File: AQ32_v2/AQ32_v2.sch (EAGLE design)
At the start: 115 parts, among them Q2 BCV27, Q3 BCV27, Q5 BCV27, Q6 BCV27, U1 ITG-3200, U10 MS5611, U11 MIC5239, U13 74AHC1G86DCK, U2 STM32F10XVXT6, U3 74AHC1G86DCK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

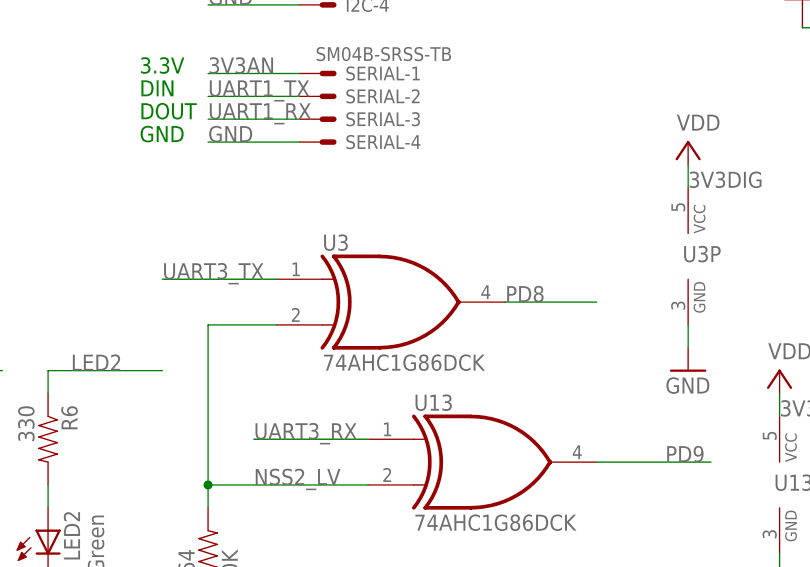
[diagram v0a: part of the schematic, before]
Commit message: fixed SBUS Tx connection, fixed clearance issue with updated XOR connections, added extra vias for ground
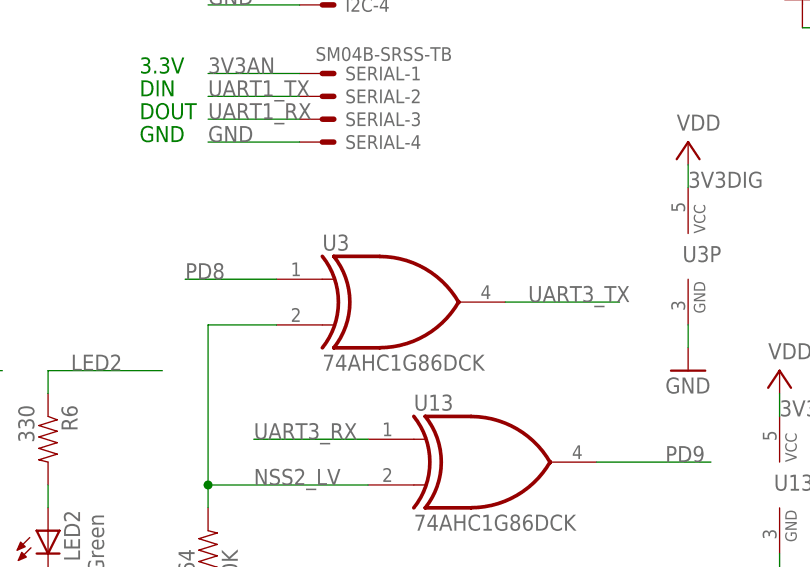
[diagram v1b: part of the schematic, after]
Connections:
- net PD8: now also U3A.I0; no longer U3A.O
- net UART3_TX: now also U3A.O; no longer U3A.I0
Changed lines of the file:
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@@
 </segment>
 <segment>
-<pinref part="U3" gate="A" pin="I0"/>
-<wire x1="83.82" y1="45.72" x2="71.12" y2="45.72" width="0.1524" layer="91"/>
-<label x="71.12" y="45.72" size="1.778" layer="95"/>
+<pinref part="U3" gate="A" pin="O"/>
+<wire x1="109.22" y1="43.18" x2="121.92" y2="43.18" width="0.1524" layer="91"/>
+<label x="111.76" y="43.18" size="1.778" layer="95"/>
 </segment>
 </net>
@@
 </segment>
 <segment>
-<pinref part="U3" gate="A" pin="O"/>
-<wire x1="109.22" y1="43.18" x2="119.38" y2="43.18" width="0.1524" layer="91"/>
-<label x="109.22" y="43.18" size="1.778" layer="95"/>
-</segment>
-</net>
+<pinref part="U3" gate="A" pin="I0"/>
+<wire x1="83.82" y1="45.72" x2="73.66" y2="45.72" width="0.1524" layer="91"/>
+<label x="73.66" y="45.72" size="1.778" layer="95"/>
+</segment>
+</net>

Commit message: "j" version from Alfred
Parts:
- JP1: value (none) -> JP1; device SparkFun-Connectors:M02PTH -> SparkFun-Connectors:M02LOCK
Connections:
- net 3V3AN: now also C29.1, C45.1, U1.VDD, U10.CSB, U10.CSB@2, U10.PS, U10.VDD; no longer I2C-1.S, JP1-2.7, JP1-2.8, SERIAL-1.S
- net 3V3DIG: now also I2C-1.S, JP1-2.7, JP1-2.8, SERIAL-1.S; no longer C29.1, C45.1, U1.VDD, U10.CSB, U10.CSB@2, U10.PS, U10.VDD
- net LEDGND1: now also Q2.C; no longer Q5.C
- net LEDGND2: now also Q5.C; no longer Q2.C
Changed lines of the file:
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@@
 <part name="U10" library="DSP-TI" deviceset="MS5611" device=""/>
 <part name="SUPPLY19" library="supply2" deviceset="GND" device=""/>
-<part name="SUPPLY20" library="supply2" deviceset="VDD" device=""/>
 <part name="C45" library="rcl" deviceset="C-US" device="C0402" value="0.1uF"/>
 <part name="SUPPLY21" library="supply2" deviceset="GND" device=""/>
@@
 <part name="GND25" library="SparkFun" deviceset="GND" device=""/>
 <part name="SUPPLY2" library="supply2" deviceset="V+" device="" value="VDD"/>
-<part name="JP1" library="SparkFun-Connectors" deviceset="M02" device="PTH"/>
+<part name="JP1" library="SparkFun-Connectors" deviceset="M02" device="LOCK" value="JP1"/>
+<part name="P+4" library="SparkFun" deviceset="3.3V" device="" value="VDDA"/>
 </parts>
 <sheets>
@@
 <instance part="U10" gate="G$1" x="307.34" y="33.02"/>
 <instance part="SUPPLY19" gate="GND" x="309.88" y="10.16"/>
-<instance part="SUPPLY20" gate="G$1" x="309.88" y="60.96"/>
 <instance part="C45" gate="G$1" x="325.12" y="50.8"/>
 <instance part="SUPPLY21" gate="GND" x="325.12" y="40.64"/>
@@
 <instance part="SUPPLY2" gate="1" x="129.54" y="60.96"/>
 <instance part="JP1" gate="G$1" x="17.78" y="99.06"/>
+<instance part="P+4" gate="G$1" x="309.88" y="58.42"/>
 </instances>
 <busses>
@@
 <pinref part="R3" gate="G$1" pin="1"/>
 <pinref part="GND15" gate="1" pin="GND"/>
-<pinref part="JP1" gate="G$1" pin="1"/>
 <wire x1="33.02" y1="73.66" x2="33.02" y2="71.12" width="0.1524" layer="91"/>
 <wire x1="25.4" y1="99.06" x2="27.94" y2="99.06" width="0.1524" layer="91"/>
@@
 <wire x1="27.94" y1="73.66" x2="33.02" y2="73.66" width="0.1524" layer="91"/>
 <junction x="33.02" y="73.66"/>
+<pinref part="JP1" gate="G$1" pin="1"/>
 </segment>
 <segment>
@@
 </segment>
 <segment>
-<pinref part="SERIAL" gate="-1" pin="S"/>
-<wire x1="86.36" y1="68.58" x2="76.2" y2="68.58" width="0.1524" layer="91"/>
-<label x="76.2" y="68.58" size="1.778" layer="95"/>
-</segment>
-<segment>
-<pinref part="I2C" gate="-1" pin="S"/>
-<wire x1="86.36" y1="83.82" x2="76.2" y2="83.82" width="0.1524" layer="91"/>
-<label x="76.2" y="83.82" size="1.778" layer="95"/>
-</segment>
-<segment>
-<pinref part="JP1-2" gate="G$1" pin="8"/>
-<wire x1="429.26" y1="76.2" x2="436.88" y2="76.2" width="0.1524" layer="91"/>
-<label x="429.26" y="76.2" size="1.778" layer="95"/>
-</segment>
-<segment>
-<pinref part="JP1-2" gate="G$1" pin="7"/>
-<wire x1="429.26" y1="73.66" x2="436.88" y2="73.66" width="0.1524" layer="91"/>
-<label x="429.26" y="73.66" size="1.778" layer="95"/>
+<wire x1="309.88" y1="58.42" x2="309.88" y2="55.88" width="0.1524" layer="91"/>
+<wire x1="309.88" y1="55.88" x2="309.88" y2="50.8" width="0.1524" layer="91"/>
+<wire x1="309.88" y1="55.88" x2="325.12" y2="55.88" width="0.1524" layer="91"/>
+<wire x1="325.12" y1="55.88" x2="325.12" y2="53.34" width="0.1524" layer="91"/>
+<junction x="309.88" y="55.88"/>
+<pinref part="U10" gate="G$1" pin="VDD"/>
+<pinref part="C45" gate="G$1" pin="1"/>
+<label x="309.88" y="58.42" size="1.778" layer="95"/>
+<wire x1="309.88" y1="55.88" x2="281.94" y2="55.88" width="0.1524" layer="91"/>
+<wire x1="281.94" y1="55.88" x2="281.94" y2="40.64" width="0.1524" layer="91"/>
+<pinref part="U10" gate="G$1" pin="CSB@2"/>
+<wire x1="281.94" y1="40.64" x2="281.94" y2="38.1" width="0.1524" layer="91"/>
+<wire x1="281.94" y1="38.1" x2="281.94" y2="35.56" width="0.1524" layer="91"/>
+<wire x1="281.94" y1="35.56" x2="292.1" y2="35.56" width="0.1524" layer="91"/>
+<pinref part="U10" gate="G$1" pin="CSB"/>
+<wire x1="292.1" y1="38.1" x2="281.94" y2="38.1" width="0.1524" layer="91"/>
+<pinref part="U10" gate="G$1" pin="PS"/>
+<wire x1="292.1" y1="40.64" x2="281.94" y2="40.64" width="0.1524" layer="91"/>
+<junction x="281.94" y="40.64"/>
+<junction x="281.94" y="38.1"/>
+<pinref part="P+4" gate="G$1" pin="3.3V"/>
+</segment>
+<segment>
+<wire x1="342.9" y1="157.48" x2="327.66" y2="157.48" width="0.1524" layer="91"/>
+<wire x1="342.9" y1="157.48" x2="342.9" y2="149.86" width="0.1524" layer="91"/>
+<junction x="327.66" y="157.48"/>
+<label x="330.2" y="157.48" size="1.778" layer="95"/>
+<pinref part="U1" gate="G$1" pin="VDD"/>
+<pinref part="C29" gate="G$1" pin="1"/>
 </segment>
 </net>
@@
 </segment>
 <segment>
-<wire x1="309.88" y1="58.42" x2="309.88" y2="55.88" width="0.1524" layer="91"/>
-<wire x1="309.88" y1="55.88" x2="309.88" y2="50.8" width="0.1524" layer="91"/>
-<wire x1="309.88" y1="55.88" x2="325.12" y2="55.88" width="0.1524" layer="91"/>
-<wire x1="325.12" y1="55.88" x2="325.12" y2="53.34" width="0.1524" layer="91"/>
-<junction x="309.88" y="55.88"/>
-<pinref part="SUPPLY20" gate="G$1" pin="VDD"/>
-<pinref part="U10" gate="G$1" pin="VDD"/>
-<pinref part="C45" gate="G$1" pin="1"/>
-<label x="309.88" y="58.42" size="1.778" layer="95"/>
-<wire x1="309.88" y1="55.88" x2="281.94" y2="55.88" width="0.1524" layer="91"/>
-<wire x1="281.94" y1="55.88" x2="281.94" y2="40.64" width="0.1524" layer="91"/>
-<pinref part="U10" gate="G$1" pin="CSB@2"/>
-<wire x1="281.94" y1="40.64" x2="281.94" y2="38.1" width="0.1524" layer="91"/>
-<wire x1="281.94" y1="38.1" x2="281.94" y2="35.56" width="0.1524" layer="91"/>
-<wire x1="281.94" y1="35.56" x2="292.1" y2="35.56" width="0.1524" layer="91"/>
-<pinref part="U10" gate="G$1" pin="CSB"/>
-<wire x1="292.1" y1="38.1" x2="281.94" y2="38.1" width="0.1524" layer="91"/>
-<pinref part="U10" gate="G$1" pin="PS"/>
-<wire x1="292.1" y1="40.64" x2="281.94" y2="40.64" width="0.1524" layer="91"/>
-<junction x="281.94" y="40.64"/>
-<junction x="281.94" y="38.1"/>
-</segment>
-<segment>
-<wire x1="342.9" y1="157.48" x2="327.66" y2="157.48" width="0.1524" layer="91"/>
-<wire x1="342.9" y1="157.48" x2="342.9" y2="149.86" width="0.1524" layer="91"/>
-<junction x="327.66" y="157.48"/>
-<label x="330.2" y="157.48" size="1.778" layer="95"/>
-<pinref part="U1" gate="G$1" pin="VDD"/>
-<pinref part="C29" gate="G$1" pin="1"/>
-</segment>
-<segment>
 <wire x1="261.62" y1="170.18" x2="261.62" y2="175.26" width="0.1524" layer="91"/>
 <label x="259.08" y="175.26" size="1.778" layer="95"/>
@@
 <pinref part="U3" gate="P" pin="VCC"/>
 <label x="129.54" y="55.88" size="1.778" layer="95"/>
+</segment>
+<segment>
+<pinref part="I2C" gate="-1" pin="S"/>
+<wire x1="86.36" y1="83.82" x2="76.2" y2="83.82" width="0.1524" layer="91"/>
+<label x="76.2" y="83.82" size="1.778" layer="95"/>
+</segment>
+<segment>
+<pinref part="SERIAL" gate="-1" pin="S"/>
+<wire x1="86.36" y1="68.58" x2="76.2" y2="68.58" width="0.1524" layer="91"/>
+<label x="76.2" y="68.58" size="1.778" layer="95"/>
+</segment>
+<segment>
+<pinref part="JP1-2" gate="G$1" pin="8"/>
+<wire x1="429.26" y1="76.2" x2="436.88" y2="76.2" width="0.1524" layer="91"/>
+<label x="429.26" y="76.2" size="1.778" layer="95"/>
+</segment>
+<segment>
+<pinref part="JP1-2" gate="G$1" pin="7"/>
+<wire x1="429.26" y1="73.66" x2="436.88" y2="73.66" width="0.1524" layer="91"/>
+<label x="429.26" y="73.66" size="1.778" layer="95"/>
 </segment>
 </net>
@@
 <net name="LEDGND1" class="0">
 <segment>
+<pinref part="JP4-1" gate="G$1" pin="1"/>
+<wire x1="495.3" y1="25.4" x2="505.46" y2="25.4" width="0.1524" layer="91"/>
+<label x="495.3" y="25.4" size="1.778" layer="95"/>
+</segment>
+<segment>
+<wire x1="30.48" y1="33.02" x2="27.94" y2="33.02" width="0.1524" layer="91"/>
+<pinref part="Q2" gate="G$1" pin="C"/>
+<label x="27.94" y="33.02" size="1.778" layer="95"/>
+</segment>
+</net>
+<net name="LEDGND2" class="0">
+<segment>
+<pinref part="JP4-1" gate="G$1" pin="2"/>
+<wire x1="495.3" y1="27.94" x2="505.46" y2="27.94" width="0.1524" layer="91"/>
+<label x="495.3" y="27.94" size="1.778" layer="95"/>
+</segment>
+<segment>
 <wire x1="30.48" y1="45.72" x2="27.94" y2="45.72" width="0.1524" layer="91"/>
 <pinref part="Q5" gate="G$1" pin="C"/>
 <label x="27.94" y="45.72" size="1.778" layer="95"/>
 </segment>
-<segment>
-<pinref part="JP4-1" gate="G$1" pin="1"/>
-<wire x1="495.3" y1="25.4" x2="505.46" y2="25.4" width="0.1524" layer="91"/>
-<label x="495.3" y="25.4" size="1.778" layer="95"/>
-</segment>
-</net>
-<net name="LEDGND2" class="0">
-<segment>
-<wire x1="30.48" y1="33.02" x2="27.94" y2="33.02" width="0.1524" layer="91"/>
-<pinref part="Q2" gate="G$1" pin="C"/>
-<label x="27.94" y="33.02" size="1.778" layer="95"/>
-</segment>
-<segment>
-<pinref part="JP4-1" gate="G$1" pin="2"/>
-<wire x1="495.3" y1="27.94" x2="505.46" y2="27.94" width="0.1524" layer="91"/>
-<label x="495.3" y="27.94" size="1.778" layer="95"/>
-</segment>
-</net>
+</net>

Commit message: change LED connector type for normal 100mil pitch
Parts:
- JP1, JP4-1, JP4-2: device SparkFun-Connectors:M02LOCK -> SparkFun-Connectors:M02PTH
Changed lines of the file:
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@@
 <part name="OSD" library="con-jst2" deviceset="?M07B-SRSS-TB" device="S"/>
 <part name="L2" library="SparkFun" deviceset="INDUCTOR" device="0805" value="22uH"/>
-<part name="JP4-1" library="SparkFun-Connectors" deviceset="M02" device="LOCK" value="JP4"/>
-<part name="JP4-2" library="SparkFun-Connectors" deviceset="M02" device="LOCK" value="JP4"/>
+<part name="JP4-1" library="SparkFun-Connectors" deviceset="M02" device="PTH" value="JP4"/>
+<part name="JP4-2" library="SparkFun-Connectors" deviceset="M02" device="PTH" value="JP4"/>
 <part name="JP3-1" library="SparkFun-Connectors" deviceset="M09" device=""/>
 <part name="JP3-2" library="SparkFun-Connectors" deviceset="M09" device=""/>
@@
 <part name="GND25" library="SparkFun" deviceset="GND" device=""/>
 <part name="SUPPLY2" library="supply2" deviceset="V+" device="" value="VDD"/>
-<part name="JP1" library="SparkFun-Connectors" deviceset="M02" device="LOCK" value="JP1"/>
+<part name="JP1" library="SparkFun-Connectors" deviceset="M02" device="PTH" value="JP1"/>
 <part name="P+4" library="SparkFun" deviceset="3.3V" device="" value="VDDA"/>
 </parts>

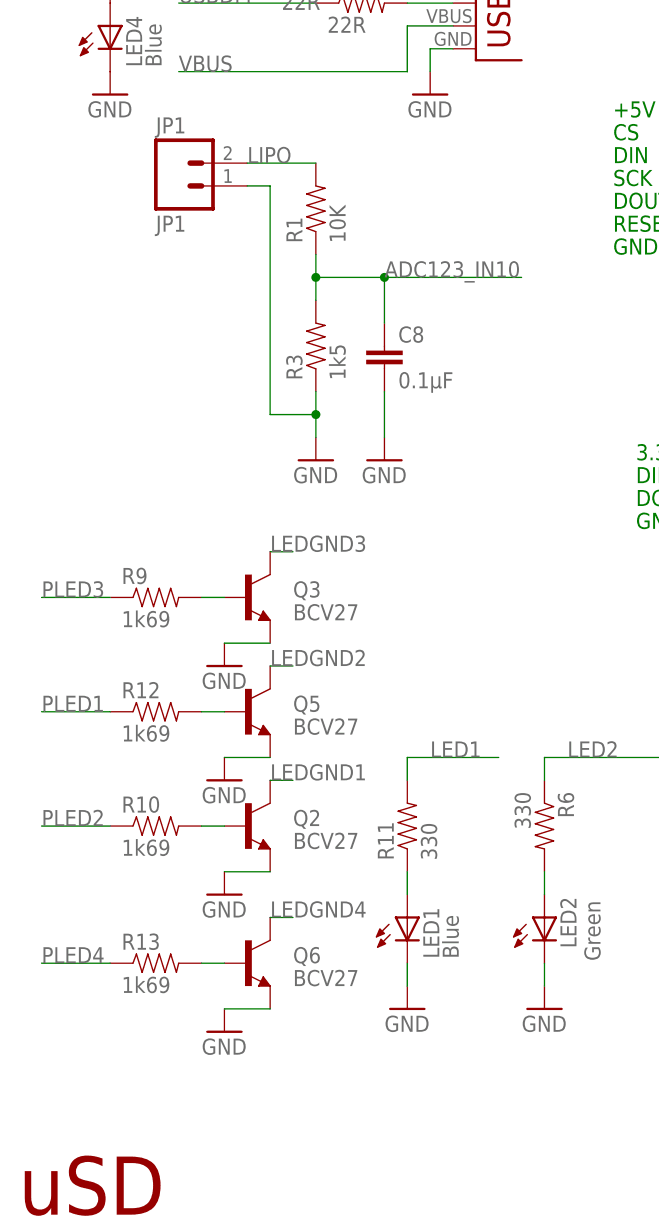
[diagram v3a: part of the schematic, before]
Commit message: Isolate BM/LED GND from main GND using 0R resistor. More clearance around holes.
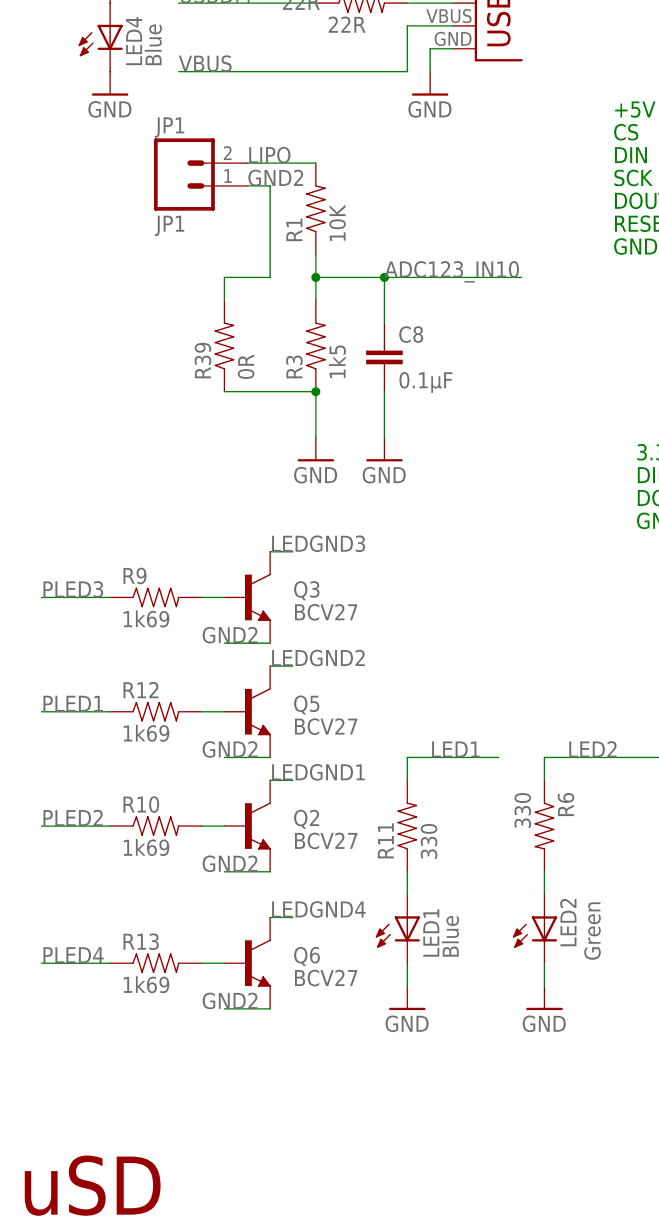
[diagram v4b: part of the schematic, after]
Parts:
- added R39: 0R, SparkFun:RESISTOR0402
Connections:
- new net GND2: JP1.1, Q2.E, Q3.E, Q5.E, Q6.E, R39.2
- net GND: now also R39.1; no longer JP1.1, Q2.E, Q3.E, Q5.E, Q6.E
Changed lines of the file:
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@@
 <part name="GND16" library="supply1" deviceset="GND" device=""/>
 <part name="SUPPLY7" library="supply2" deviceset="VDD" device=""/>
-<part name="GND47" library="SparkFun" deviceset="GND" device=""/>
-<part name="GND48" library="SparkFun" deviceset="GND" device=""/>
-<part name="GND49" library="SparkFun" deviceset="GND" device=""/>
-<part name="GND50" library="SparkFun" deviceset="GND" device=""/>
 <part name="U13" library="74xx-little-us" deviceset="74*1G86" device="DCK" technology="AHC"/>
 <part name="GND51" library="SparkFun" deviceset="GND" device=""/>
@@
 <part name="JP1" library="SparkFun-Connectors" deviceset="M02" device="PTH" value="JP1"/>
 <part name="P+4" library="SparkFun" deviceset="3.3V" device="" value="VDDA"/>
+<part name="R39" library="SparkFun" deviceset="RESISTOR" device="0402" value="0R"/>
 </parts>
 <sheets>
@@
 <instance part="GND16" gate="1" x="124.46" y="-55.88"/>
 <instance part="SUPPLY7" gate="G$1" x="147.32" y="-25.4"/>
-<instance part="GND47" gate="1" x="22.86" y="5.08"/>
-<instance part="GND48" gate="1" x="22.86" y="20.32"/>
-<instance part="GND49" gate="1" x="22.86" y="33.02"/>
-<instance part="GND50" gate="1" x="22.86" y="45.72"/>
 <instance part="U13" gate="A" x="106.68" y="25.4"/>
 <instance part="U13" gate="P" x="139.7" y="22.86"/>
@@
 <instance part="JP1" gate="G$1" x="17.78" y="99.06"/>
 <instance part="P+4" gate="G$1" x="309.88" y="58.42"/>
+<instance part="R39" gate="G$1" x="22.86" y="81.28" rot="R90"/>
 </instances>
 <busses>
@@
 </segment>
 <segment>
-<wire x1="33.02" y1="76.2" x2="33.02" y2="73.66" width="0.1524" layer="91"/>
+<pinref part="GND15" gate="1" pin="GND"/>
 <pinref part="R3" gate="G$1" pin="1"/>
-<pinref part="GND15" gate="1" pin="GND"/>
-<wire x1="33.02" y1="73.66" x2="33.02" y2="71.12" width="0.1524" layer="91"/>
-<wire x1="25.4" y1="99.06" x2="27.94" y2="99.06" width="0.1524" layer="91"/>
-<wire x1="27.94" y1="99.06" x2="27.94" y2="73.66" width="0.1524" layer="91"/>
-<wire x1="27.94" y1="73.66" x2="33.02" y2="73.66" width="0.1524" layer="91"/>
-<junction x="33.02" y="73.66"/>
-<pinref part="JP1" gate="G$1" pin="1"/>
+<wire x1="33.02" y1="76.2" x2="33.02" y2="71.12" width="0.1524" layer="91"/>
+<pinref part="R39" gate="G$1" pin="1"/>
+<wire x1="33.02" y1="76.2" x2="22.86" y2="76.2" width="0.1524" layer="91"/>
+<junction x="33.02" y="76.2"/>
 </segment>
 <segment>
@@
 <junction x="124.46" y="-43.18"/>
 <label x="132.08" y="-35.56" size="1.778" layer="95"/>
-</segment>
-<segment>
-<wire x1="22.86" y1="7.62" x2="27.94" y2="7.62" width="0.1524" layer="91"/>
-<pinref part="Q6" gate="G$1" pin="E"/>
-<pinref part="GND47" gate="1" pin="GND"/>
-</segment>
-<segment>
-<wire x1="22.86" y1="22.86" x2="27.94" y2="22.86" width="0.1524" layer="91"/>
-<pinref part="Q2" gate="G$1" pin="E"/>
-<pinref part="GND48" gate="1" pin="GND"/>
-</segment>
-<segment>
-<wire x1="22.86" y1="35.56" x2="27.94" y2="35.56" width="0.1524" layer="91"/>
-<pinref part="Q5" gate="G$1" pin="E"/>
-<pinref part="GND49" gate="1" pin="GND"/>
-</segment>
-<segment>
-<wire x1="22.86" y1="48.26" x2="27.94" y2="48.26" width="0.1524" layer="91"/>
-<pinref part="Q3" gate="G$1" pin="E"/>
-<pinref part="GND50" gate="1" pin="GND"/>
 </segment>
 <segment>
@@
 </segment>
 </net>
+<net name="GND2" class="1">
+<segment>
+<wire x1="25.4" y1="99.06" x2="27.94" y2="99.06" width="0.1524" layer="91"/>
+<pinref part="JP1" gate="G$1" pin="1"/>
+<label x="25.4" y="99.06" size="1.778" layer="95"/>
+<wire x1="27.94" y1="99.06" x2="27.94" y2="88.9" width="0.1524" layer="91"/>
+<pinref part="R39" gate="G$1" pin="2"/>
+<wire x1="27.94" y1="88.9" x2="22.86" y2="88.9" width="0.1524" layer="91"/>
+<wire x1="22.86" y1="88.9" x2="22.86" y2="86.36" width="0.1524" layer="91"/>
+</segment>
+<segment>
+<wire x1="22.86" y1="48.26" x2="27.94" y2="48.26" width="0.1524" layer="91"/>
+<pinref part="Q3" gate="G$1" pin="E"/>
+<label x="20.32" y="48.26" size="1.778" layer="95"/>
+</segment>
+<segment>
+<wire x1="22.86" y1="35.56" x2="27.94" y2="35.56" width="0.1524" layer="91"/>
+<pinref part="Q5" gate="G$1" pin="E"/>
+<label x="20.32" y="35.56" size="1.778" layer="95"/>
+</segment>
+<segment>
+<wire x1="22.86" y1="22.86" x2="27.94" y2="22.86" width="0.1524" layer="91"/>
+<pinref part="Q2" gate="G$1" pin="E"/>
+<label x="20.32" y="22.86" size="1.778" layer="95"/>
+</segment>
+<segment>
+<wire x1="22.86" y1="7.62" x2="27.94" y2="7.62" width="0.1524" layer="91"/>
+<pinref part="Q6" gate="G$1" pin="E"/>
+<label x="20.32" y="7.62" size="1.778" layer="95"/>
+</segment>
+</net>
